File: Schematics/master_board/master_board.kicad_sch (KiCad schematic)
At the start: 7 parts

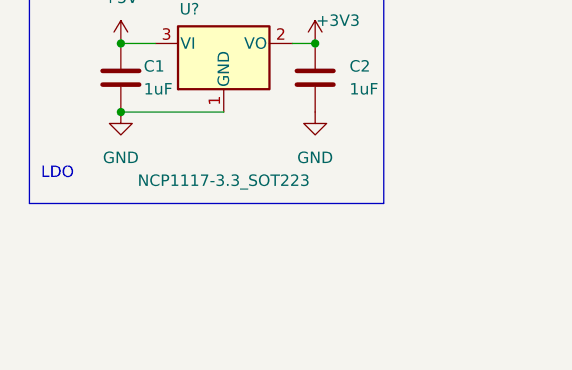
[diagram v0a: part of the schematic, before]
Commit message: Added reset tactile switch, pulled up
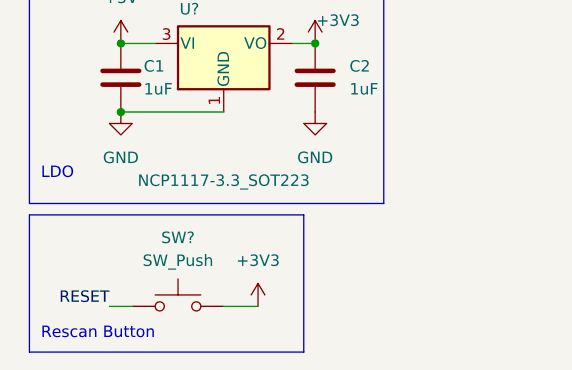
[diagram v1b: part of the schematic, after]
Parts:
- added SW?: SW_Push, symbol Switch:SW_Push
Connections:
- net +3V3: now also SW?.2
- new net RESET: SW?.1
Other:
- note added: "Rescan Button"
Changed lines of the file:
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@@
+    (stroke (width 0) (type default) (color 0 0 0 0))
+  )
+  (wire (pts (xy 24.13 134.62) (xy 26.67 134.62))
+    (stroke (width 0) (type default) (color 0 0 0 0))
+  )
+  (wire (pts (xy 36.83 134.62) (xy 40.64 134.62))
     (stroke (width 0) (type default) (color 0 0 0 0))
   )
@@
     (stroke (width 0) (type default) (color 0 0 0 0))
   )
+  (polyline (pts (xy 45.72 139.7) (xy 15.24 139.7))
+    (stroke (width 0) (type default) (color 0 0 0 0))
+  )
   (polyline (pts (xy 60.96 13.97) (xy 102.87 13.97))
     (stroke (width 0) (type default) (color 0 0 0 0))
@@
     (stroke (width 0) (type default) (color 0 0 0 0))
   )
+  (polyline (pts (xy 15.24 124.46) (xy 45.72 124.46))
+    (stroke (width 0) (type default) (color 0 0 0 0))
+  )
   (polyline (pts (xy 59.69 97.79) (xy 15.24 97.79))
     (stroke (width 0) (type default) (color 0 0 0 0))
@@
     (stroke (width 0) (type default) (color 0 0 0 0))
   )
+  (polyline (pts (xy 15.24 124.46) (xy 15.24 139.7))
+    (stroke (width 0) (type default) (color 0 0 0 0))
+  )
+  (polyline (pts (xy 45.72 124.46) (xy 45.72 139.7))
+    (stroke (width 0) (type default) (color 0 0 0 0))
+  )
   (wire (pts (xy 43.18 38.1) (xy 43.18 39.37))
     (stroke (width 0) (type default) (color 0 0 0 0))
@@
     (effects (font (size 1.27 1.27)) (justify left bottom))
   )
+  (text "Rescan Button" (at 16.51 138.43 0)
+    (effects (font (size 1.27 1.27)) (justify left bottom))
+  )
   (text "LDO" (at 16.51 120.65 0)
     (effects (font (size 1.27 1.27)) (justify left bottom))
   )
+  (label "RESET" (at 24.13 134.62 180)
+    (effects (font (size 1.27 1.27)) (justify right bottom))
+  )
   (label "SWDIO" (at 71.12 19.05 0)
     (effects (font (size 1.27 1.27)) (justify left bottom))
@@
   (label "USB_DP" (at 45.72 38.1 0)
     (effects (font (size 1.27 1.27)) (justify left bottom))
+  )
+  (symbol (lib_name "+3V3_1") (lib_id "power:+3V3") (at 40.64 134.62 0) (unit 1)
+    (in_bom yes) (on_board yes) (fields_autoplaced)
+    (property "Reference" "#PWR?" (id 0) (at 40.64 138.43 0)
+      (effects (font (size 1.27 1.27)) hide)
+    )
+    (property "Value" "+3V3" (id 1) (at 40.64 129.54 0))
+    (property "Footprint" "" (id 2) (at 40.64 134.62 0)
+      (effects (font (size 1.27 1.27)) hide)
+    )
+    (property "Datasheet" "" (id 3) (at 40.64 134.62 0)
+      (effects (font (size 1.27 1.27)) hide)
+    )
+    (pin "1")
   )
   (symbol (lib_id "Device:C") (at 25.4 109.22 0) (unit 1)
@@
     (pin "3")
   )
+  (symbol (lib_id "Switch:SW_Push") (at 31.75 134.62 0) (unit 1)
+    (in_bom yes) (on_board yes) (fields_autoplaced)
+    (property "Reference" "SW?" (id 0) (at 31.75 127 0))
+    (property "Value" "SW_Push" (id 1) (at 31.75 129.54 0))
+    (property "Footprint" "" (id 2) (at 31.75 129.54 0)
+      (effects (font (size 1.27 1.27)) hide)
+    )
+    (property "Datasheet" "~" (id 3) (at 31.75 129.54 0)
+      (effects (font (size 1.27 1.27)) hide)
+    )
+    (pin "1")
+    (pin "2")
+  )
   (symbol (lib_id "power:+3V3") (at 46.99 105.41 0) (unit 1)
     (in_bom yes) (on_board yes)
@@
   )
   (symbol_instances
+    (path "/2d953bb2-6f49-498c-8baa-987aa8c48f44"
+      (reference "#PWR?") (unit 1) (value "+3V3") (footprint "")
+    )
     (path "/4dd72ae5-5e23-4752-8360-9e6720bd1bcb"
       (reference "#PWR?") (unit 1) (value "GND") (footprint "")
@@
       (reference "R2") (unit 1) (value "5k1") (footprint "")
     )
+    (path "/a524c91f-ff5d-4073-ae0f-6cfe00c0490f"
+      (reference "SW?") (unit 1) (value "SW_Push") (footprint "")
+    )
     (path "/990f8f52-6648-46f6-bbad-aaa69d08df8c"

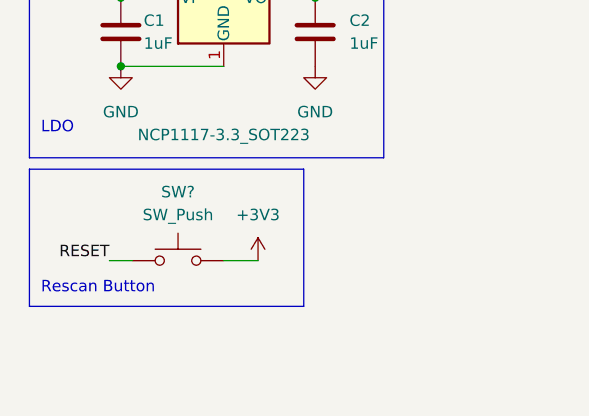
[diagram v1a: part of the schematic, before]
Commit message: Added Accelerometer/Gyroscope Component
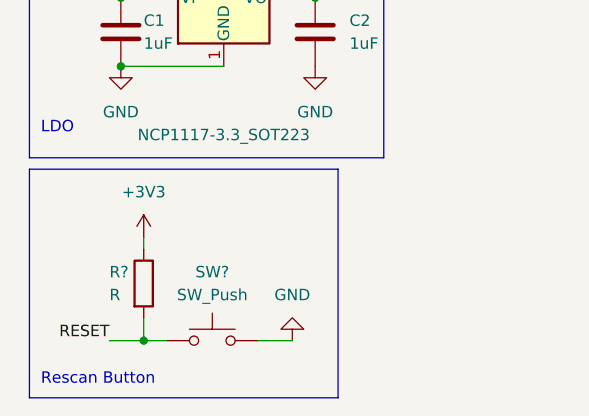
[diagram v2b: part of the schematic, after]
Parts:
- added R?: R, symbol Device:R
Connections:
- net +3V3: now also R?.1; no longer SW?.2
- net GND: now also SW?.2
- net RESET: now also R?.2
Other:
- moved on the sheet: SW?
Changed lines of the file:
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@@
   (junction (at 43.18 38.1) (diameter 0) (color 0 0 0 0)
   )
+  (junction (at 27.94 143.51) (diameter 0) (color 0 0 0 0)
+  )
   (junction (at 24.13 90.17) (diameter 0) (color 0 0 0 0)
   )
@@
   (junction (at 46.99 105.41) (diameter 0) (color 0 0 0 0)
   )
+  (wire (pts (xy 27.94 143.51) (xy 30.48 143.51))
+    (stroke (width 0) (type default) (color 0 0 0 0))
+  )
   (polyline (pts (xy 102.87 29.21) (xy 60.96 29.21))
     (stroke (width 0) (type default) (color 0 0 0 0))
@@
     (stroke (width 0) (type default) (color 0 0 0 0))
   )
-  (wire (pts (xy 24.13 134.62) (xy 26.67 134.62))
-    (stroke (width 0) (type default) (color 0 0 0 0))
-  )
-  (wire (pts (xy 36.83 134.62) (xy 40.64 134.62))
+  (wire (pts (xy 24.13 143.51) (xy 27.94 143.51))
+    (stroke (width 0) (type default) (color 0 0 0 0))
+  )
+  (wire (pts (xy 40.64 143.51) (xy 44.45 143.51))
     (stroke (width 0) (type default) (color 0 0 0 0))
   )
@@
     (stroke (width 0) (type default) (color 0 0 0 0))
   )
+  (wire (pts (xy 27.94 132.08) (xy 27.94 133.35))
+    (stroke (width 0) (type default) (color 0 0 0 0))
+  )
   (wire (pts (xy 25.4 105.41) (xy 29.21 105.41))
     (stroke (width 0) (type default) (color 0 0 0 0))
@@
     (stroke (width 0) (type default) (color 0 0 0 0))
   )
-  (polyline (pts (xy 45.72 139.7) (xy 15.24 139.7))
+  (polyline (pts (xy 49.53 149.86) (xy 15.24 149.86))
     (stroke (width 0) (type default) (color 0 0 0 0))
   )
@@
     (stroke (width 0) (type default) (color 0 0 0 0))
   )
-  (polyline (pts (xy 15.24 124.46) (xy 45.72 124.46))
+  (polyline (pts (xy 15.24 124.46) (xy 49.53 124.46))
     (stroke (width 0) (type default) (color 0 0 0 0))
   )
@@
     (stroke (width 0) (type default) (color 0 0 0 0))
   )
-  (polyline (pts (xy 15.24 124.46) (xy 15.24 139.7))
-    (stroke (width 0) (type default) (color 0 0 0 0))
-  )
-  (polyline (pts (xy 45.72 124.46) (xy 45.72 139.7))
+  (polyline (pts (xy 15.24 124.46) (xy 15.24 149.86))
+    (stroke (width 0) (type default) (color 0 0 0 0))
+  )
+  (polyline (pts (xy 49.53 124.46) (xy 49.53 149.86))
     (stroke (width 0) (type default) (color 0 0 0 0))
   )
@@
     (stroke (width 0) (type default) (color 0 0 0 0))
   )
+  (wire (pts (xy 27.94 140.97) (xy 27.94 143.51))
+    (stroke (width 0) (type default) (color 0 0 0 0))
+  )
   (wire (pts (xy 25.4 113.03) (xy 36.83 113.03))
     (stroke (width 0) (type default) (color 0 0 0 0))
@@
     (effects (font (size 1.27 1.27)) (justify left bottom))
   )
-  (text "Rescan Button" (at 16.51 138.43 0)
+  (text "Rescan Button" (at 16.51 148.59 0)
     (effects (font (size 1.27 1.27)) (justify left bottom))
   )
@@
     (effects (font (size 1.27 1.27)) (justify left bottom))
   )
-  (label "RESET" (at 24.13 134.62 180)
+  (label "RESET" (at 24.13 143.51 180)
     (effects (font (size 1.27 1.27)) (justify right bottom))
   )
@@
   (label "USB_DP" (at 45.72 38.1 0)
     (effects (font (size 1.27 1.27)) (justify left bottom))
-  )
-  (symbol (lib_name "+3V3_1") (lib_id "power:+3V3") (at 40.64 134.62 0) (unit 1)
-    (in_bom yes) (on_board yes) (fields_autoplaced)
-    (property "Reference" "#PWR?" (id 0) (at 40.64 138.43 0)
-      (effects (font (size 1.27 1.27)) hide)
-    )
-    (property "Value" "+3V3" (id 1) (at 40.64 129.54 0))
-    (property "Footprint" "" (id 2) (at 40.64 134.62 0)
-      (effects (font (size 1.27 1.27)) hide)
-    )
-    (property "Datasheet" "" (id 3) (at 40.64 134.62 0)
-      (effects (font (size 1.27 1.27)) hide)
-    )
-    (pin "1")
   )
   (symbol (lib_id "Device:C") (at 25.4 109.22 0) (unit 1)
@@
     (pin "S1")
   )
+  (symbol (lib_id "Device:R") (at 27.94 137.16 0) (unit 1)
+    (in_bom yes) (on_board yes)
+    (property "Reference" "R?" (id 0) (at 24.13 135.89 0)
+      (effects (font (size 1.27 1.27)) (justify left))
+    )
+    (property "Value" "R" (id 1) (at 24.13 138.43 0)
+      (effects (font (size 1.27 1.27)) (justify left))
+    )
+    (property "Footprint" "" (id 2) (at 26.162 137.16 90)
+      (effects (font (size 1.27 1.27)) hide)
+    )
+    (property "Datasheet" "~" (id 3) (at 27.94 137.16 0)
+      (effects (font (size 1.27 1.27)) hide)
+    )
+    (pin "1")
+    (pin "2")
+  )
   (symbol (lib_id "power:GND") (at 24.13 90.17 0) (unit 1)
     (in_bom yes) (on_board yes) (fields_autoplaced)
@@
     (pin "1")
   )
+  (symbol (lib_name "+3V3_1") (lib_id "power:+3V3") (at 27.94 132.08 0) (unit 1)
+    (in_bom yes) (on_board yes) (fields_autoplaced)
+    (property "Reference" "#PWR?" (id 0) (at 27.94 135.89 0)
+      (effects (font (size 1.27 1.27)) hide)
+    )
+    (property "Value" "+3V3" (id 1) (at 27.94 127 0))
+    (property "Footprint" "" (id 2) (at 27.94 132.08 0)
+      (effects (font (size 1.27 1.27)) hide)
+    )
+    (property "Datasheet" "" (id 3) (at 27.94 132.08 0)
+      (effects (font (size 1.27 1.27)) hide)
+    )
+    (pin "1")
+  )
   (symbol (lib_id "Connector:Conn_01x03_Female") (at 81.28 21.59 0) (unit 1)
     (in_bom yes) (on_board yes) (fields_autoplaced)
@@
     (pin "3")
   )
-  (symbol (lib_id "Switch:SW_Push") (at 31.75 134.62 0) (unit 1)
-    (in_bom yes) (on_board yes) (fields_autoplaced)
-    (property "Reference" "SW?" (id 0) (at 31.75 127 0))
-    (property "Value" "SW_Push" (id 1) (at 31.75 129.54 0))
-    (property "Footprint" "" (id 2) (at 31.75 129.54 0)
-      (effects (font (size 1.27 1.27)) hide)
-    )
-    (property "Datasheet" "~" (id 3) (at 31.75 129.54 0)
+  (symbol (lib_id "Switch:SW_Push") (at 35.56 143.51 0) (unit 1)
+    (in_bom yes) (on_board yes) (fields_autoplaced)
+    (property "Reference" "SW?" (id 0) (at 35.56 135.89 0))
+    (property "Value" "SW_Push" (id 1) (at 35.56 138.43 0))
+    (property "Footprint" "" (id 2) (at 35.56 138.43 0)
+      (effects (font (size 1.27 1.27)) hide)
+    )
+    (property "Datasheet" "~" (id 3) (at 35.56 138.43 0)
       (effects (font (size 1.27 1.27)) hide)
     )
@@
     (pin "3")
   )
+  (symbol (lib_name "GND_1") (lib_id "power:GND") (at 44.45 143.51 180) (unit 1)
+    (in_bom yes) (on_board yes) (fields_autoplaced)
+    (property "Reference" "#PWR?" (id 0) (at 44.45 137.16 0)
+      (effects (font (size 1.27 1.27)) hide)
+    )
+    (property "Value" "GND" (id 1) (at 44.45 138.43 0))
+    (property "Footprint" "" (id 2) (at 44.45 143.51 0)
+      (effects (font (size 1.27 1.27)) hide)
+    )
+    (property "Datasheet" "" (id 3) (at 44.45 143.51 0)
+      (effects (font (size 1.27 1.27)) hide)
+    )
+    (pin "1")
+  )
   (symbol (lib_id "power:GND") (at 69.85 21.59 270) (unit 1)
     (in_bom yes) (on_board yes) (fields_autoplaced)
@@
   )
   (symbol_instances
-    (path "/2d953bb2-6f49-498c-8baa-987aa8c48f44"
-      (reference "#PWR?") (unit 1) (value "+3V3") (footprint "")
-    )
     (path "/4dd72ae5-5e23-4752-8360-9e6720bd1bcb"
       (reference "#PWR?") (unit 1) (value "GND") (footprint "")
@@
       (reference "#PWR?") (unit 1) (value "+5V") (footprint "")
     )
+    (path "/93a508d0-64ca-4ca9-b5db-bce74295e4ed"
+      (reference "#PWR?") (unit 1) (value "+3V3") (footprint "")
+    )
     (path "/ac910ee8-1a5b-48ca-9f4c-515fc31f9f6a"
       (reference "#PWR?") (unit 1) (value "+3V3") (footprint "")
@@
       (reference "#PWR?") (unit 1) (value "GND") (footprint "")
     )
+    (path "/f3cba786-006d-4a3c-a63b-1e446ab7fe61"
+      (reference "#PWR?") (unit 1) (value "GND") (footprint "")
+    )
     (path "/f7e20034-c89f-4aad-adb8-e994ac5a0ff6"
       (reference "#PWR?") (unit 1) (value "GND") (footprint "")
@@
       (reference "R2") (unit 1) (value "5k1") (footprint "")
     )
+    (path "/55bba71c-5909-4883-b4ed-8246b4bb2d87"
+      (reference "R?") (unit 1) (value "R") (footprint "")
+    )
     (path "/a524c91f-ff5d-4073-ae0f-6cfe00c0490f"
